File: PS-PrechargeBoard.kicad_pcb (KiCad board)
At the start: 2 copper layers, 230 parts, among them IC1 LM74502DDFR, IC2 TCAN3413DR, J1 HV_Main, J10 SWD, J2 HV_Motor, J3 DIAG, J4 CAN_IN, J5 CAN_OUT, J6 DEBUG_NANO, J7 PRECHARGE_CTRL, J8 USB_C_Receptacle_USB2.0_16P, J9 SWD_Header, K1 DE1a-12V, K2 DE1a-12V, Q1 NMOS, Q2 NMOS, Q3 PSMN012-100YS, Q4 PSMN012-100YS, SW1 Reset, SW2 SW_SPDT, U1 TLV9002QDRQ1, U4 TLV9002QDRQ1, U7 MCP1826S, U8 STM32G473CETx, Y1 Crystal

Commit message: usb-c placement
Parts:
- moved D11 104.8 mm to (184.8, 64.5), turned to 180 degrees
- moved R70 104.6 mm to (176.2, 67.6), turned to 90 degrees
- moved C50 102.4 mm to (189.3, 66.8), turned to 180 degrees
- moved R69 98.9 mm to (176.1, 70.9), turned to 90 degrees
- moved D12 95.0 mm to (181.7, 64.8), turned to 90 degrees
- moved J8 92.4 mm to (182.2, 70.6)
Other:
- board text added: "USB-C"

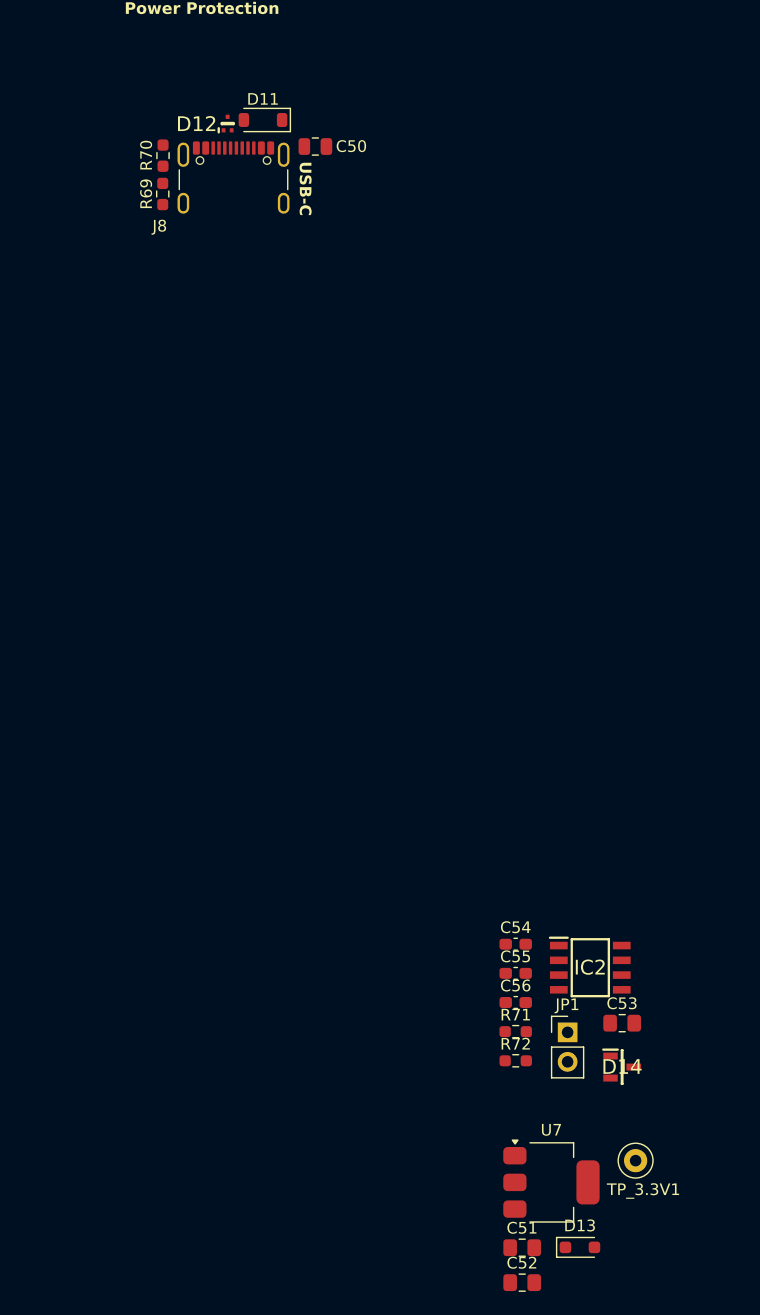
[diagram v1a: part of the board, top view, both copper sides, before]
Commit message: 10k ohm resistor to precharge gate
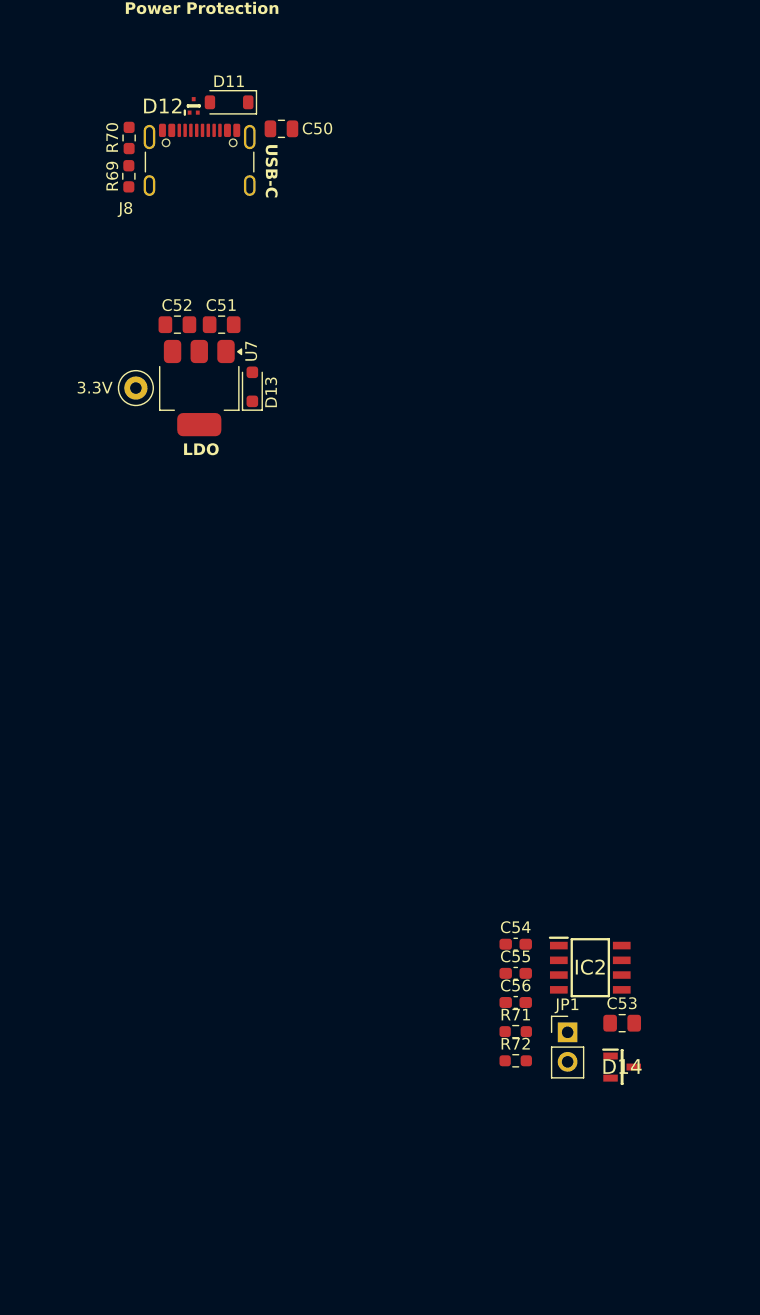
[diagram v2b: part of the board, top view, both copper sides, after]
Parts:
- moved C52 87.7 mm to (177.4, 82.1), turned to 180 degrees
- moved C51 83.6 mm to (181.2, 82.1)
- moved D13 79.3 mm to (183.9, 87.5), turned to 90 degrees
- moved TP_3.3V1 79.3 mm to (173.8, 87.6)
- moved U7 74.9 mm to (179.3, 87.6), turned to -90 degrees
- moved R70 3.29 mm to (173.3, 66.1)
- moved D11 3.29 mm to (181.9, 63.0)
- moved C50 3.29 mm to (186.4, 65.3)
- moved D12 3.29 mm to (178.8, 63.3)
- moved J8 3.29 mm to (179.3, 69.1)
- moved R69 3.29 mm to (173.2, 69.4)
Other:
- board text added: "LDO"

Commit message: updated voltage divider to amc3311
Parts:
- added R81: 10k, Resistor_SMD:R_0603_1608Metric_Pad0.98x0.95mm_HandSolder, F.Cu at (272.1, 37.6)
- added R82: 1k, Resistor_SMD:R_0603_1608Metric_Pad0.98x0.95mm_HandSolder, F.Cu at (272.1, 40.1)
- R11, R12, R13, R14, R37, R38, R39, R42, R43, R44, R6, R7, R8, R9: value 100k -> 174k
- R32: value 50 -> 10k
- R36: value 100k -> 50; footprint Resistor_SMD:R_1206_3216Metric_Pad1.30x1.75mm_HandSolder -> Precharge_Board:RES_PWR263S-35-3300F
- R40, R45: value 10k -> 174k; footprint Resistor_SMD:R_0603_1608Metric_Pad0.98x0.95mm_HandSolder -> Resistor_SMD:R_1206_3216Metric_Pad1.30x1.75mm_HandSolder
- R41: value 100k -> 10k; footprint Resistor_SMD:R_1206_3216Metric_Pad1.30x1.75mm_HandSolder -> Resistor_SMD:R_0603_1608Metric_Pad0.98x0.95mm_HandSolder
- R54: value 10 -> 10k
- R58, R61: value 47k -> 10
- R59: value 10 -> 47k
- R62: value 0 -> 47k
- R64: value 33 -> 0
- R65: value 100k -> 10k
- R66: value 7.32k -> 33
- R68: value 15.8k -> 7.32k
- R69: value 5.1k -> 100k
- R70: value 5.1k -> 15.8k
- R71, R72: value 60 -> 5.1k
- R73: value 1k -> 60
- R74: value 10k -> 60
- R76: value 1k -> 10k
- R77, R78: value 22 -> 1k
- R79: value 10k -> 22
- R80: value 1k -> 22
- moved JP1 39.7 mm to (234.1, 110.7)
- moved D14 28.2 mm to (222.4, 118.7)
- moved IC2 21.8 mm to (210.0, 116.0)
- moved C53 19.7 mm to (206.4, 125.0)
- moved C54 17.7 mm to (200.6, 118.9)
- moved C55 14.8 mm to (201.1, 124.3)
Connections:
- Q1 pad 2: /MAINPRECHARGE_CTRL -> Net-(Q1-G)
- Q2 pad 2: /MOTPRECHARGE_CTRL -> Net-(Q2-G)
- R32 pad 1: /MOT_RES_HV- -> /MAINPRECHARGE_CTRL
- R32 pad 2: MOT_HV+ -> Net-(Q1-G)
- R32 pad 3: /Motor_Fuse/RESISTOR -> (no net)
- R36 pad 1: MOT_HV+ -> /MOT_RES_HV-
- R36 pad 2: Net-(R36-Pad2) -> MOT_HV+
- R37 pad 1: Net-(R36-Pad2) -> MOT_HV+
- R39 pad 2: /Motor_VoltageSensor/V_IN+ -> Net-(R39-Pad2)
- R40 pad 1: /Motor_VoltageSensor/V_IN+ -> Net-(R39-Pad2)
- R40 pad 2: HVGND -> /Motor_VoltageSensor/V_IN+
- R41 pad 1: MOT_HV- -> /Motor_VoltageSensor/V_IN+
- R41 pad 2: Net-(R41-Pad2) -> HVGND
- R42 pad 1: Net-(R41-Pad2) -> MOT_HV-
- R44 pad 2: /Motor_VoltageSensor/V_IN- -> Net-(R44-Pad2)
- R45 pad 1: /Motor_VoltageSensor/V_IN- -> Net-(R44-Pad2)
- R45 pad 2: HVGND -> /Motor_VoltageSensor/V_IN-
- R46 pad 1: /Motor_VoltageSensor/OUTP_HV+ -> /Motor_VoltageSensor/V_IN-
- R46 pad 2: Net-(U4A-+) -> HVGND
- R47 pad 1: Net-(U4A-+) -> /Motor_VoltageSensor/OUTP_HV+
- R47 pad 2: GND -> Net-(U4A-+)
- R48 pad 1: /Motor_VoltageSensor/OUTN_HV+ -> Net-(U4A-+)
- R48 pad 2: Net-(U4A--) -> GND
- R49 pad 1: /Motor_VoltageSensor/OUTP_HV- -> /Motor_VoltageSensor/OUTN_HV+
- R49 pad 2: Net-(U4B-+) -> Net-(U4A--)
- R50 pad 1: Net-(U4B-+) -> /Motor_VoltageSensor/OUTP_HV-
- R50 pad 2: GND -> Net-(U4B-+)
- R51 pad 1: /Motor_VoltageSensor/OUTN_HV- -> Net-(U4B-+)
- R51 pad 2: Net-(U4B--) -> GND
- R52 pad 1: Net-(U4A--) -> /Motor_VoltageSensor/OUTN_HV-
- R52 pad 2: Net-(R52-Pad2) -> Net-(U4B--)
- R53 pad 1: Net-(U4B--) -> Net-(U4A--)
- R54 pad 1: Net-(R52-Pad2) -> Net-(U4B--)
- R54 pad 2: /MOT_V+ -> Net-(R54-Pad2)
- R55 pad 2: /MOT_V- -> /MOT_V+
- R56 pad 1: /Motor_VoltageSensor/VoltageSensor_HV+/OUTN -> Net-(R54-Pad2)
- R56 pad 2: /Motor_VoltageSensor/OUTN_HV+ -> /MOT_V-
- R57 pad 1: /Motor_VoltageSensor/VoltageSensor_HV+/OUTP -> /Motor_VoltageSensor/VoltageSensor_HV+/OUTN
- R57 pad 2: /Motor_VoltageSensor/OUTP_HV+ -> /Motor_VoltageSensor/OUTN_HV+
- R58 pad 1: 3V3 -> /Motor_VoltageSensor/VoltageSensor_HV+/OUTP
- R58 pad 2: /MOT_DIAG -> /Motor_VoltageSensor/OUTP_HV+
- R59 pad 1: /Motor_VoltageSensor/VoltageSensor_HV-/OUTN -> 3V3
- R59 pad 2: /Motor_VoltageSensor/OUTN_HV- -> /MOT_DIAG
- R60 pad 1: /Motor_VoltageSensor/VoltageSensor_HV-/OUTP -> /Motor_VoltageSensor/VoltageSensor_HV-/OUTN
- R60 pad 2: /Motor_VoltageSensor/OUTP_HV- -> /Motor_VoltageSensor/OUTN_HV-
- R61 pad 1: 3V3 -> /Motor_VoltageSensor/VoltageSensor_HV-/OUTP
- R61 pad 2: /MOT_DIAG -> /Motor_VoltageSensor/OUTP_HV-
- R62 pad 1: /VIN_FUSED -> 3V3
- R62 pad 2: /VIN_PROT -> /MOT_DIAG
- R63 pad 1: Net-(D10-K) -> /MOTPRECHARGE_CTRL
- R63 pad 2: /VIN_FUSED -> Net-(Q2-G)
- R64 pad 1: Net-(C46-Pad1) -> /VIN_FUSED
- R64 pad 2: /LV Power/PowerProtection/gate -> /VIN_PROT
- R65 pad 1: /VIN_FUSED -> Net-(D10-K)
- R65 pad 2: /LV Power/PowerProtection/OV -> /VIN_FUSED
- R66 pad 1: /LV Power/PowerProtection/OV -> Net-(C46-Pad1)
- R66 pad 2: GND -> /LV Power/PowerProtection/gate
- R67 pad 2: /LV Power/PowerProtection/EN/UVLO -> /LV Power/PowerProtection/OV
- R68 pad 1: GND -> /LV Power/PowerProtection/OV
- R68 pad 2: /LV Power/PowerProtection/EN/UVLO -> GND
- R69 pad 1: GND -> /VIN_FUSED
- R69 pad 2: /LV Power/USB-C_Connector/CC1 -> /LV Power/PowerProtection/EN/UVLO
- R70 pad 2: /LV Power/USB-C_Connector/CC2 -> /LV Power/PowerProtection/EN/UVLO
- R71 pad 1: /BPS_CAN_H -> GND
- R71 pad 2: Net-(C56-Pad2) -> /LV Power/USB-C_Connector/CC1
- R72 pad 1: Net-(C56-Pad2) -> GND
- R72 pad 2: Net-(JP1-A) -> /LV Power/USB-C_Connector/CC2
- R73 pad 1: Net-(D15-Pad2) -> /BPS_CAN_H
- R73 pad 2: GND -> Net-(C56-Pad2)
- R74 pad 1: /48PinMCU/NRST -> Net-(C56-Pad2)
- R74 pad 2: 3V3 -> Net-(JP1-A)
- R75 pad 1: Net-(D15-Pad4) -> Net-(D15-Pad2)
- R76 pad 1: Net-(D15-Pad6) -> /48PinMCU/NRST
- R76 pad 2: GND -> 3V3
- R77 pad 1: /48PinMCU/SWCLK -> Net-(D15-Pad4)
- R77 pad 2: Net-(J10-Pin_3) -> GND
- R78 pad 1: /48PinMCU/SWDIO -> Net-(D15-Pad6)
- R78 pad 2: Net-(J10-Pin_4) -> GND
- R79 pad 1: /48PinMCU/BOOT0 -> /48PinMCU/SWCLK
- R79 pad 2: Net-(D16-A2) -> Net-(J10-Pin_3)
- R80 pad 1: Net-(D17-K) -> /48PinMCU/SWDIO
- R80 pad 2: GND -> Net-(J10-Pin_4)
- U4 pad 1: Net-(R52-Pad2) -> Net-(R53-Pad2)
- U4 pad 7: Net-(R53-Pad2) -> Net-(R54-Pad2)

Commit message: fixed hv placement
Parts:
- removed TP23: V_OUT+, TestPoint:TestPoint_Loop_D1.80mm_Drill1.0mm_Beaded
- removed TP24: V_OUT-, TestPoint:TestPoint_Loop_D1.80mm_Drill1.0mm_Beaded
- D12: value TPD2EUSB30DRTR -> SP0503BAHT; footprint LHRS_ICs:TPD2EUSB30DRTR -> Package_TO_SOT_SMD:SOT-143
- R32: footprint Precharge_Board:RES_PWR263S-35-3300F -> Resistor_SMD:R_0603_1608Metric_Pad0.98x0.95mm_HandSolder
- TP1, TP2, TP3, TP4, TP5, TP6, TP7, TP8, TP_3.3V1: footprint TestPoint:TestPoint_Loop_D1.80mm_Drill1.0mm_Beaded -> TestPoint:TestPoint_THTPad_D3.0mm_Drill1.5mm
- TP10: value MAIN_V+ -> MAIN_V-; footprint TestPoint:TestPoint_Loop_D1.80mm_Drill1.0mm_Beaded -> TestPoint:TestPoint_THTPad_D3.0mm_Drill1.5mm
- TP11: value MAIN_V- -> GND; footprint TestPoint:TestPoint_Loop_D1.80mm_Drill1.0mm_Beaded -> TestPoint:TestPoint_THTPad_D3.0mm_Drill1.5mm
- TP12: value AGND -> VIN_FUSED; footprint TestPoint:TestPoint_Loop_D1.80mm_Drill1.0mm_Beaded -> TestPoint:TestPoint_THTPad_D3.0mm_Drill1.5mm
- TP13: value VIN_FUSED -> MOT_V+; footprint TestPoint:TestPoint_Loop_D1.80mm_Drill1.0mm_Beaded -> TestPoint:TestPoint_THTPad_D3.0mm_Drill1.5mm
- TP14: value MOT_V+ -> MOT_V-; footprint TestPoint:TestPoint_Loop_D1.80mm_Drill1.0mm_Beaded -> TestPoint:TestPoint_THTPad_D3.0mm_Drill1.5mm
- TP15: value MOT_V- -> V_IN+; footprint TestPoint:TestPoint_Loop_D1.80mm_Drill1.0mm_Beaded -> TestPoint:TestPoint_THTPad_D3.0mm_Drill1.5mm
- TP16: value GND -> V_IN-; footprint TestPoint:TestPoint_Loop_D1.80mm_Drill1.0mm_Beaded -> TestPoint:TestPoint_THTPad_D3.0mm_Drill1.5mm
- TP17, TP21: value V_IN+ -> V_OUT+; footprint TestPoint:TestPoint_Loop_D1.80mm_Drill1.0mm_Beaded -> TestPoint:TestPoint_THTPad_D3.0mm_Drill1.5mm
- TP18, TP22: value V_IN- -> V_OUT-; footprint TestPoint:TestPoint_Loop_D1.80mm_Drill1.0mm_Beaded -> TestPoint:TestPoint_THTPad_D3.0mm_Drill1.5mm
- TP19: value V_OUT+ -> V_IN+; footprint TestPoint:TestPoint_Loop_D1.80mm_Drill1.0mm_Beaded -> TestPoint:TestPoint_THTPad_D3.0mm_Drill1.5mm
- TP20: value V_OUT- -> V_IN-; footprint TestPoint:TestPoint_Loop_D1.80mm_Drill1.0mm_Beaded -> TestPoint:TestPoint_THTPad_D3.0mm_Drill1.5mm
- TP9: value VDDA -> MAIN_V+; footprint TestPoint:TestPoint_Loop_D1.80mm_Drill1.0mm_Beaded -> TestPoint:TestPoint_THTPad_D3.0mm_Drill1.5mm
- moved TP15 196.8 mm to (88.6, 29.5)
- moved TP16 166.0 mm to (88.6, 48.2)
- moved R73 102.7 mm to (220.4, 146.5)
- moved R62 100.3 mm to (106.5, 110.1), turned to 0 degrees
- moved R74 98.2 mm to (232.2, 148.8)
- moved R72 82.9 mm to (181.7, 66.5)
- moved R63 80.9 mm to (106.9, 76.8), turned to 180 degrees
- moved R71 76.7 mm to (181.7, 70.5)
- moved TP20 76.6 mm to (88.7, 119.2)
- moved TP3 66.0 mm to (33.3, 57.1)
- moved TP19 62.9 mm to (88.7, 100.6)
- moved R46 49.8 mm to (78.5, 116.4)
- moved R32 46.2 mm to (106.9, 62.2), turned to 180 degrees
- moved R69 45.1 mm to (209.5, 42.6), turned to 180 degrees
- moved R70 40.5 mm to (206.2, 42.5), turned to 180 degrees
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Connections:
- C10 pad 2: AGND -> /Main_VoltageSensor/VoltageSensor_HV+/GND
- C12 pad 2: AGND -> /Main_VoltageSensor/VoltageSensor_HV+/GND
- C13 pad 1: AGND -> /Main_VoltageSensor/VoltageSensor_HV+/GND
- C18 pad 2: AGND -> /Main_VoltageSensor/VoltageSensor_HV-/GND
- C20 pad 2: AGND -> /Main_VoltageSensor/VoltageSensor_HV-/GND
- C21 pad 1: AGND -> /Main_VoltageSensor/VoltageSensor_HV-/GND
- C26 pad 1: VDDA -> 3V3
- C31 pad 2: AGND -> /Motor_VoltageSensor/VoltageSensor_HV+/GND
- C33 pad 2: AGND -> /Motor_VoltageSensor/VoltageSensor_HV+/GND
- C34 pad 1: AGND -> /Motor_VoltageSensor/VoltageSensor_HV+/GND
- C39 pad 2: AGND -> /Motor_VoltageSensor/VoltageSensor_HV-/GND
- C41 pad 2: AGND -> /Motor_VoltageSensor/VoltageSensor_HV-/GND
- C42 pad 1: AGND -> /Motor_VoltageSensor/VoltageSensor_HV-/GND
- C5 pad 1: VDDA -> 3V3
- C59 pad 1: VDDA -> /48PinMCU/VDDA
- C59 pad 2: AGND -> /48PinMCU/GNDA
- C63 pad 1: VDDA -> /48PinMCU/VDDA
- C63 pad 2: AGND -> /48PinMCU/GNDA
- C65 pad 1: VDDA -> /48PinMCU/VDDA
- C65 pad 2: AGND -> /48PinMCU/GNDA
- C67 pad 1: VDDA -> /48PinMCU/VDDA
- C67 pad 2: AGND -> /48PinMCU/GNDA
- C71 pad 1: VDDA -> /48PinMCU/VDDA
- C71 pad 2: AGND -> /48PinMCU/GNDA
- D12 pad 1: /USB_D+ -> GND
- D12 pad 2: /USB_D- -> /USB_D+
- D12 pad 3: GND -> /USB_D-
- FB1 pad 1: AGND -> /48PinMCU/GNDA
- FB2 pad 2: VDDA -> /48PinMCU/VDDA
- TP10 pad 1: /MAIN_V+ -> /MAIN_V-
- TP11 pad 1: /MAIN_V- -> GND
- TP12 pad 1: AGND -> /VIN_FUSED
- TP13 pad 1: /VIN_FUSED -> /MOT_V+
- TP14 pad 1: /MOT_V+ -> /MOT_V-
- TP15 pad 1: /MOT_V- -> /Main_VoltageSensor/V_IN+
- TP16 pad 1: GND -> /Main_VoltageSensor/V_IN-
- TP17 pad 1: /Main_VoltageSensor/V_IN+ -> /MAIN_V+
- TP18 pad 1: /Main_VoltageSensor/V_IN- -> /MAIN_V-
- TP19 pad 1: /MAIN_V+ -> /Motor_VoltageSensor/V_IN+
- TP20 pad 1: /MAIN_V- -> /Motor_VoltageSensor/V_IN-
- TP21 pad 1: /Motor_VoltageSensor/V_IN+ -> /MOT_V+
- TP22 pad 1: /Motor_VoltageSensor/V_IN- -> /MOT_V-
- TP9 pad 1: VDDA -> /MAIN_V+
- U1 pad 8: VDDA -> 3V3
- U2 pad 15: AGND -> /Main_VoltageSensor/VoltageSensor_HV+/GND
- U2 pad 9: AGND -> /Main_VoltageSensor/VoltageSensor_HV+/GND
- U3 pad 15: AGND -> /Main_VoltageSensor/VoltageSensor_HV-/GND
- U3 pad 9: AGND -> /Main_VoltageSensor/VoltageSensor_HV-/GND
- U4 pad 8: VDDA -> 3V3
- U5 pad 15: AGND -> /Motor_VoltageSensor/VoltageSensor_HV+/GND
- U5 pad 9: AGND -> /Motor_VoltageSensor/VoltageSensor_HV+/GND
- U6 pad 15: AGND -> /Motor_VoltageSensor/VoltageSensor_HV-/GND
- U6 pad 9: AGND -> /Motor_VoltageSensor/VoltageSensor_HV-/GND
- U8 pad 19: AGND -> /48PinMCU/GNDA
- U8 pad 20: VDDA -> /48PinMCU/VDDA
- U8 pad 21: VDDA -> /48PinMCU/VDDA

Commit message: restored pp placement
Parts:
- R11, R12, R13, R14, R37, R38, R39, R40, R42, R43, R44, R45, R6, R7, R8, R9: footprint Resistor_SMD:R_1206_3216Metric_Pad1.30x1.75mm_HandSolder -> Resistor_SMD:R_0603_1608Metric_Pad0.98x0.95mm_HandSolder
- R32, R63: value 10k -> 100
- R36, R5: value 50 -> 10k; footprint Precharge_Board:RES_PWR263S-35-3300F -> Resistor_SMD:R_0603_1608Metric_Pad0.98x0.95mm_HandSolder
- moved C52 194.0 mm to (330.9, 222.6), turned to 0 degrees
- moved TP_3.3V1 193.8 mm to (326.3, 229.0)
- moved C51 189.2 mm to (330.9, 219.6)
- moved R71 185.4 mm to (338.6, 169.2)
- moved C50 184.7 mm to (341.3, 158.9)
- moved J8 184.7 mm to (345.1, 165.9)
- moved D12 184.3 mm to (338.5, 166.5), turned to 90 degrees
- moved U7 183.3 mm to (323.6, 222.3), turned to 0 degrees
- moved D13 182.1 mm to (321.2, 227.9), turned to 0 degrees
- moved R72 178.8 mm to (333.1, 161.6), turned to 90 degrees
- moved D11 177.1 mm to (337.8, 158.2), turned to 180 degrees
- moved C53 166.1 mm to (346.7, 226.2)
- moved C55 157.7 mm to (337.5, 221.9)
- moved IC2 155.6 mm to (343.9, 221.4)
- moved C54 155.6 mm to (337.5, 219.4)
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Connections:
- R36 pad 1: /MOT_RES_HV- -> GND
- R36 pad 2: MOT_HV+ -> Net-(Q2-G)
- R5 pad 1: /MAIN_RES_HV- -> GND
- R5 pad 2: MAIN_HV+ -> Net-(Q1-G)
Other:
- board text added: "C:\LHRs\PS-PrechargeBoard"
- board text removed: "LDO"
- board text removed: "USB-C"
